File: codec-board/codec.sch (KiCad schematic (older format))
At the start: 32 parts, among them U301 AD1938, U302 ADM811TARTZ, Y301 24,576MHz

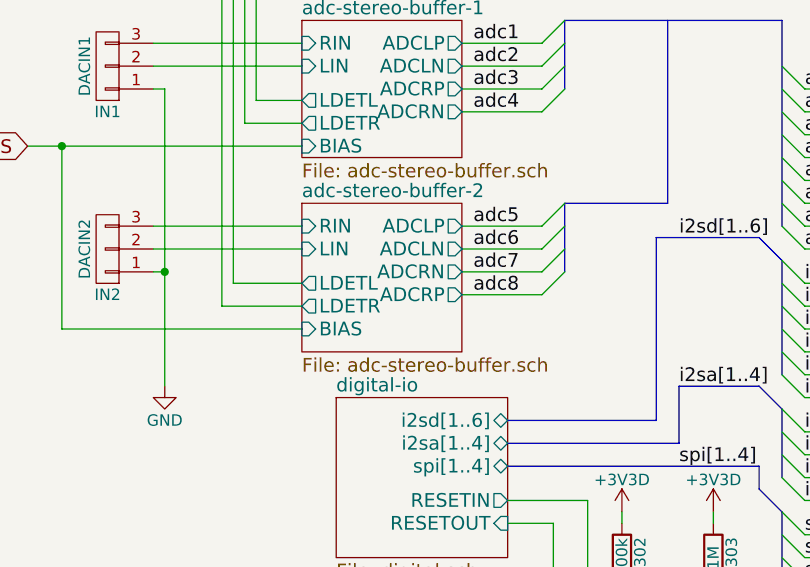
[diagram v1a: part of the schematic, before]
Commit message: fixed polarity bug on IN2
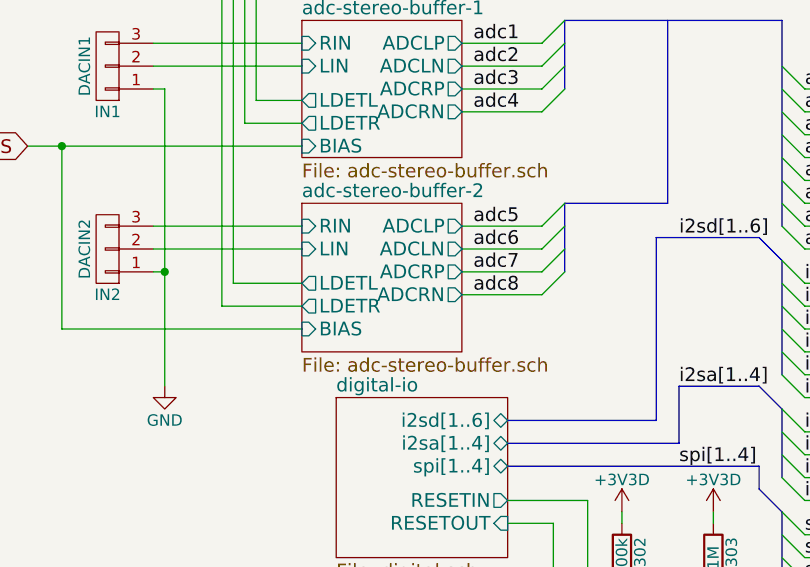
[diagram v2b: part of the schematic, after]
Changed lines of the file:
@@
 Sheet 3 10
 Title "face 2|4"
-Date "2016"
-Rev "A"
+Date "2017"
+Rev "A2"
 Comp "2015"
 Comment1 "Robert Manzke"
@@
 F2 "ADCLN" O R 3250 3350 60
 F3 "ADCLP" O R 3250 3250 60
-F4 "ADCRN" O R 3250 3450 60
-F5 "ADCRP" O R 3250 3550 60
+F4 "ADCRN" O R 3250 3550 60
+F5 "ADCRP" O R 3250 3450 60
 F6 "RIN" I L 2550 3250 60
 F7 "LIN" I L 2550 3350 60
